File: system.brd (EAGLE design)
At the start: 160 x 100 mm, 122 parts, among them IC1 TPS7B8650BQDDARQ1, IC2 TLV9101IDBVR, IC3 TLV9101IDBVR, J1 TSW-104-07-F-S, J2 163-179PH-EX, J3 RS1-02-G, SW1 1825910-6, SW2 1825910-6, SW3 1825910-6, U1 ATMEGA328PB-AU

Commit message: fixed warnings
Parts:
- SV1: value (none) -> programming pins
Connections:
- removed net N$12: U1.12
- removed net N$13: U1.13
- removed net PC_MCU_RST: TP17.TP
- net PB_MCU_RST: now also TP17.TP
- net PB_MISC1: now also U1.13
- net PB_START: now also U1.12
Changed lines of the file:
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@@
 <drawing>
 <settings>
-<setting alwaysvectorfont="yes"/>
+<setting alwaysvectorfont="no"/>
 <setting verticaltext="up"/>
 </settings>
@@
 <attribute name="VALUE" x="-22.86" y="193.04" size="1.27" layer="27"/>
 </element>
-<element name="SV1" library="con-lstb" library_urn="urn:adsk.eagle:library:162" package="MA04-1" package3d_urn="urn:adsk.eagle:package:8337/1" value="" x="-57.15" y="177.8" smashed="yes">
+<element name="SV1" library="con-lstb" library_urn="urn:adsk.eagle:library:162" package="MA04-1" package3d_urn="urn:adsk.eagle:package:8337/1" value="programming pins" x="-57.15" y="177.8" smashed="yes">
 <attribute name="MF" value="" x="-57.15" y="177.8" size="1.778" layer="27" display="off"/>
 <attribute name="MPN" value="" x="-57.15" y="177.8" size="1.778" layer="27" display="off"/>
@@
 <contactref element="SW3" pad="3"/>
 <contactref element="U1" pad="29"/>
+<contactref element="TP17" pad="TP"/>
+<wire x1="-67.31" y1="191.77" x2="-31.19" y2="159.04" width="0" layer="19" extent="1-1"/>
 <wire x1="-65.17" y1="77.91" x2="-31.19" y2="159.04" width="0" layer="19" extent="1-1"/>
 </signal>
@@
 <contactref element="SW1" pad="3"/>
 <contactref element="TP16" pad="TP"/>
+<contactref element="U1" pad="12"/>
 <wire x1="-123.9" y1="146.34" x2="-60.96" y2="191.77" width="0" layer="19" extent="1-1"/>
-</signal>
-<signal name="N$12">
-<contactref element="U1" pad="12"/>
-</signal>
-<signal name="PB_MISC1">
-<contactref element="SW2" pad="3"/>
-</signal>
-<signal name="N$13">
-<contactref element="U1" pad="13"/>
+<wire x1="-65.17" y1="69.41" x2="-123.9" y2="146.34" width="0" layer="19" extent="1-1"/>
 </signal>
 <signal name="CS_MCU">
@@
 <wire x1="-53.34" y1="177.8" x2="-35.56" y2="191.77" width="0" layer="19" extent="1-1"/>
 <wire x1="-60.52" y1="70.86" x2="-53.34" y2="177.8" width="0" layer="19" extent="1-1"/>
-</signal>
-<signal name="PC_MCU_RST">
-<contactref element="TP17" pad="TP"/>
 </signal>
 <signal name="BATTERY_AND_BUCK:N$2">
@@
 <wire x1="-111.74" y1="169.86" x2="-44.47" y2="174.94" width="0" layer="19" extent="1-1"/>
 </signal>
+<signal name="PB_MISC1">
+<contactref element="SW2" pad="3"/>
+<contactref element="U1" pad="13"/>
+<wire x1="-64.37" y1="69.41" x2="-17.22" y2="157.77" width="0" layer="19" extent="1-1"/>
+</signal>
 </signals>

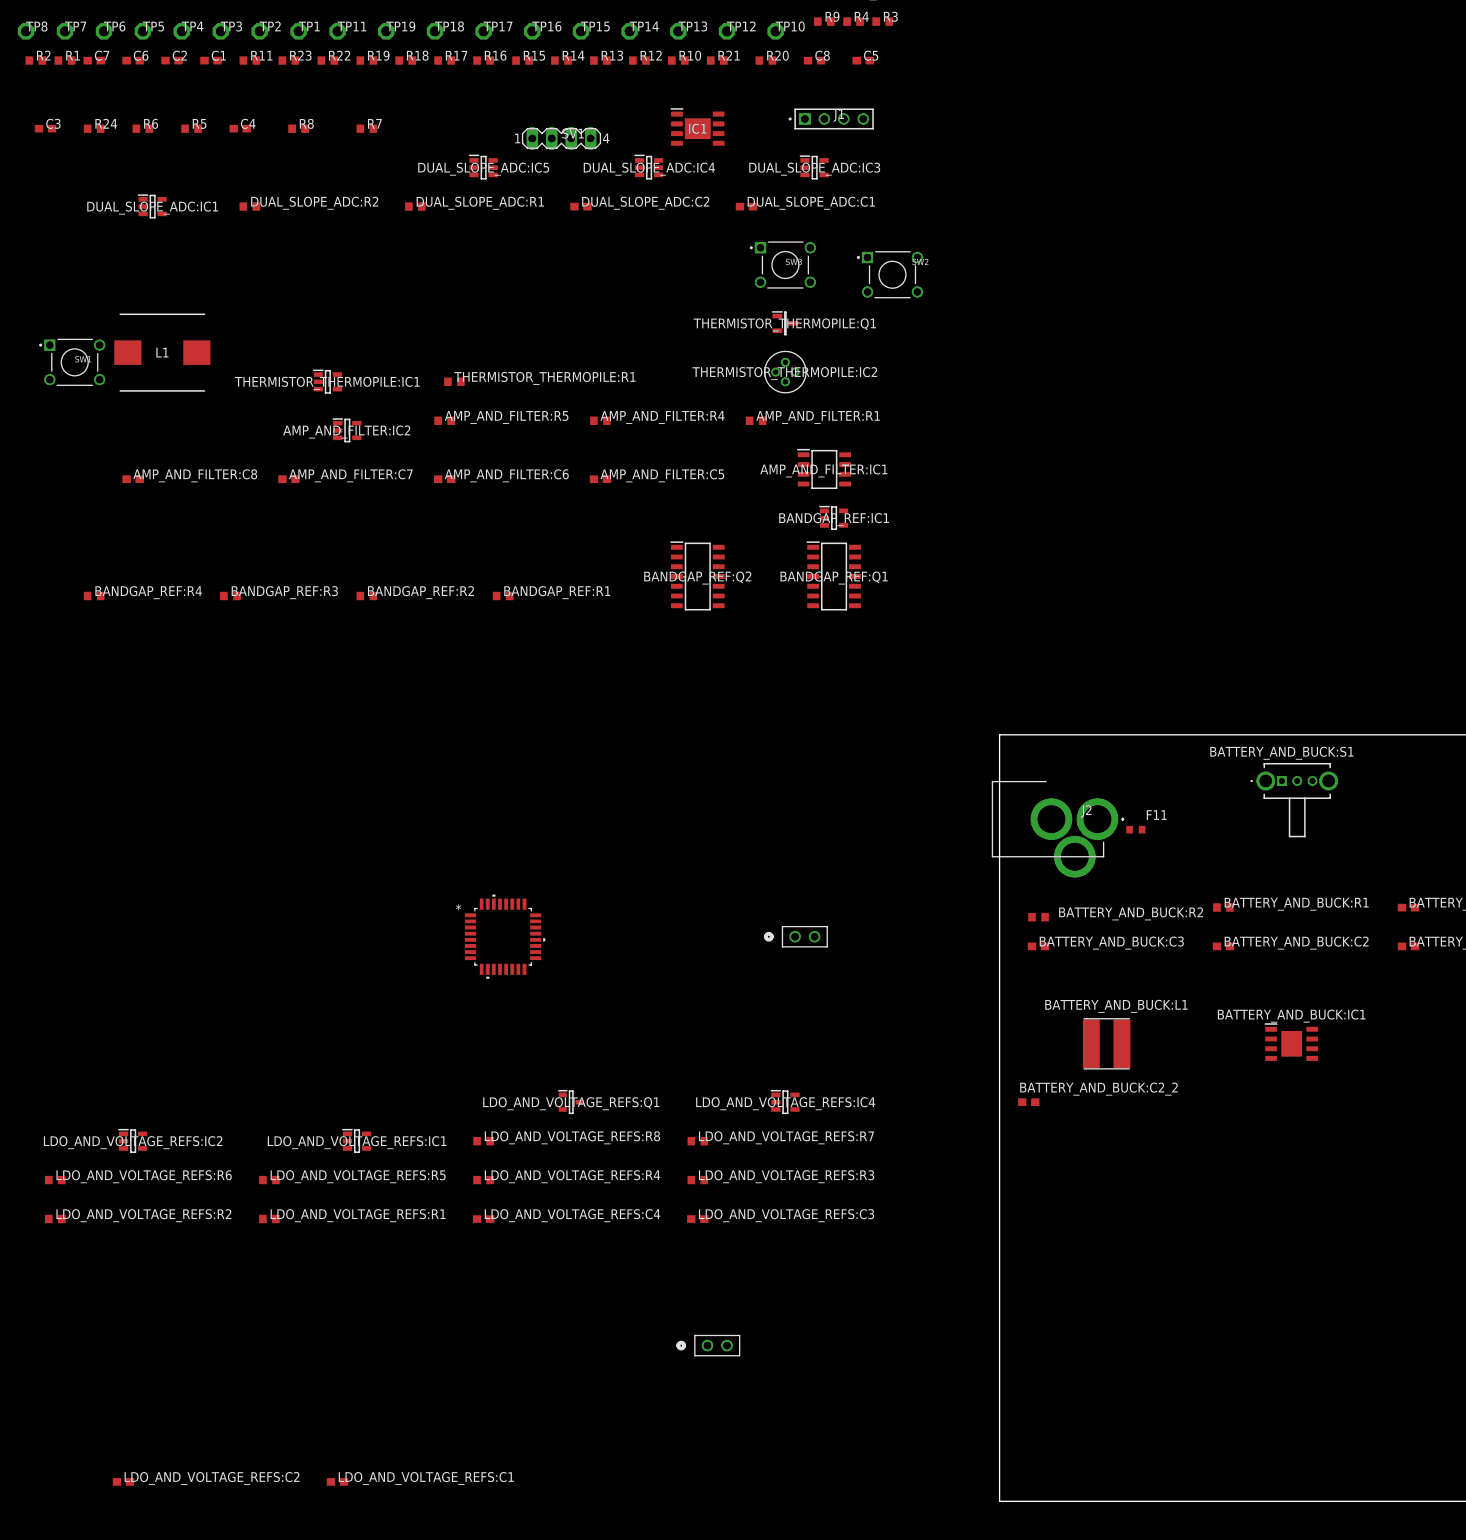
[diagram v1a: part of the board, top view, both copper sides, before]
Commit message: added cap to 2.5V reference
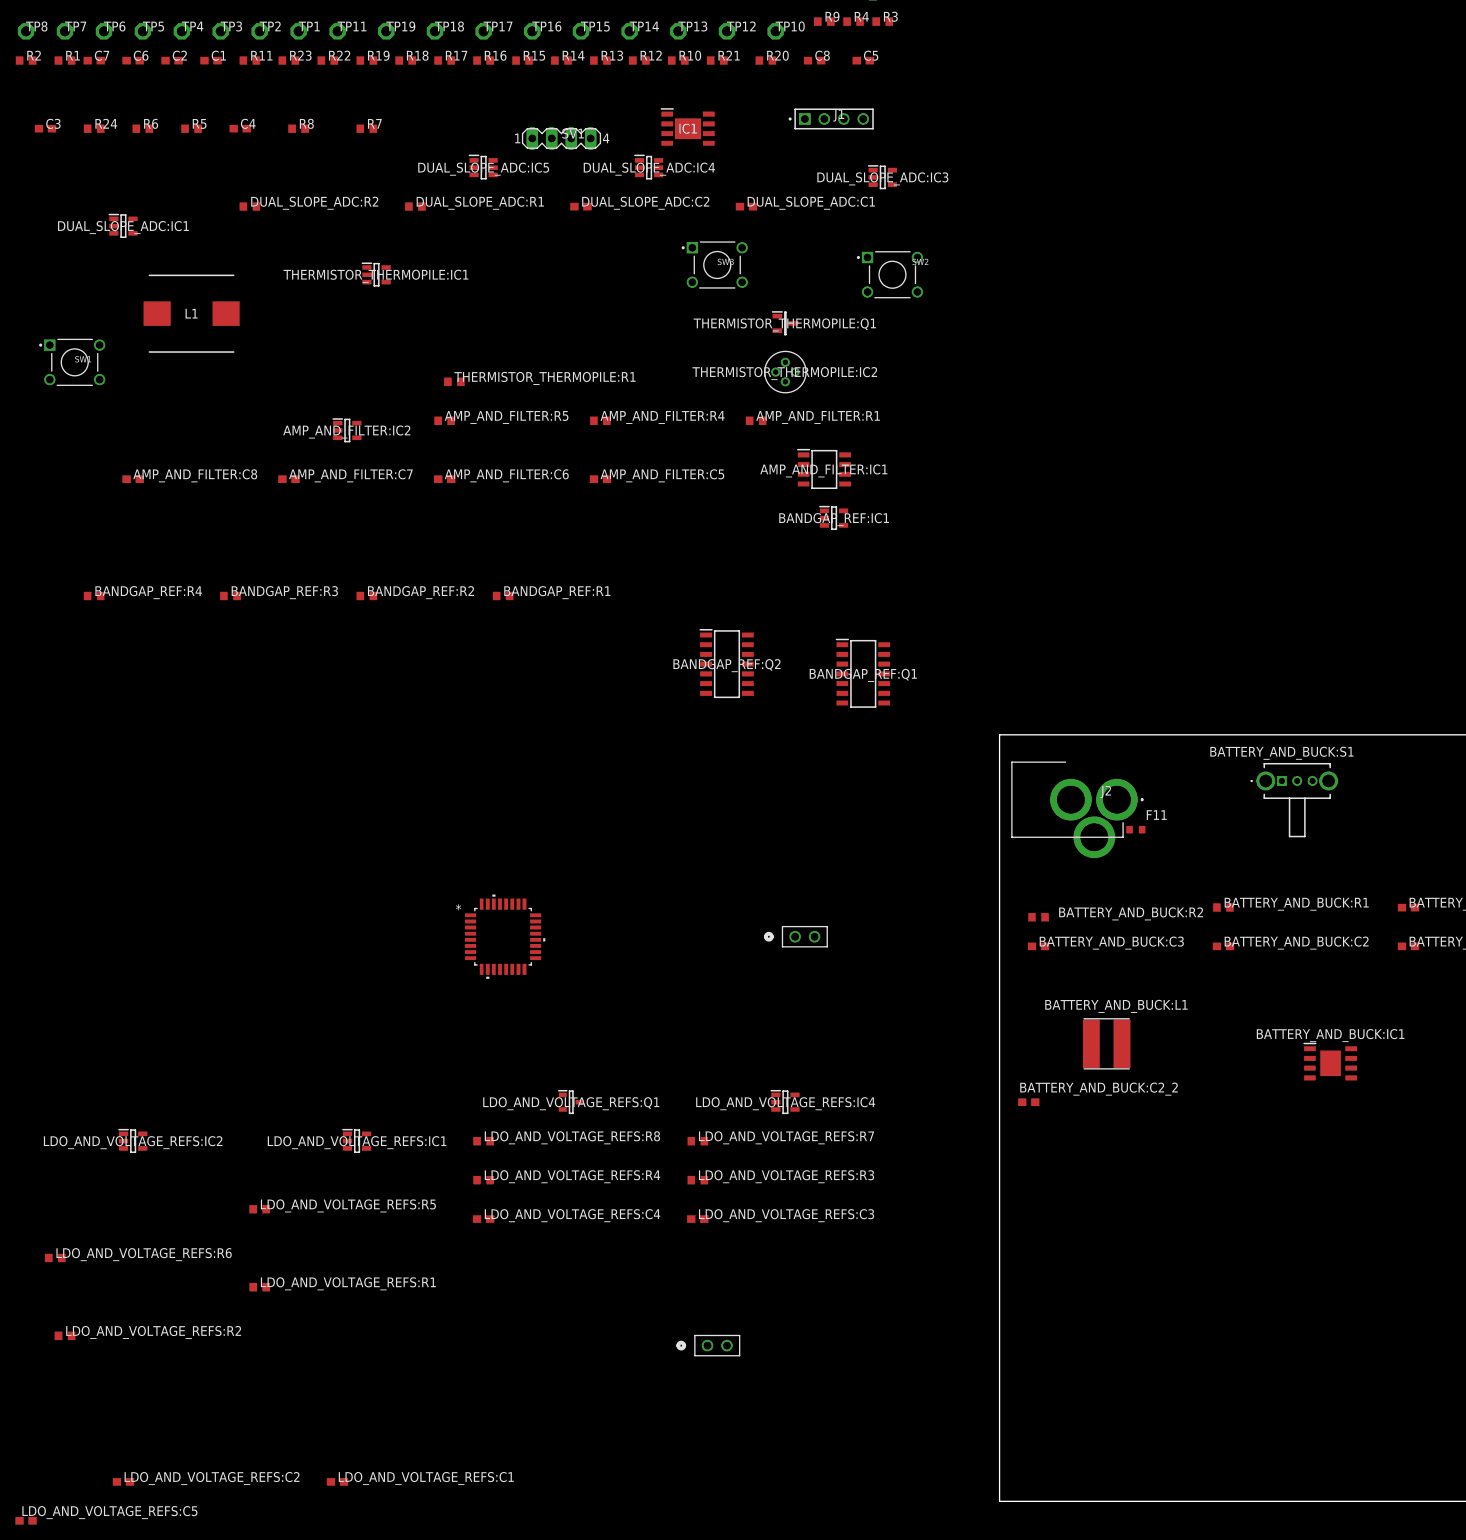
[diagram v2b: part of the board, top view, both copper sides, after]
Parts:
- added LDO_AND_VOLTAGE_REFS:C5: 1uF, rcl:C0603
- moved THERMISTOR_THERMOPILE:IC1 15.3 mm to (-81.3, 160.0)
- moved LDO_AND_VOLTAGE_REFS:R2 15.3 mm to (-121.9, 21.6)
- moved BANDGAP_REF:Q1 13.3 mm to (-17.8, 108.0)
- moved BANDGAP_REF:Q2 12.0 mm to (-35.6, 109.2)
- moved LDO_AND_VOLTAGE_REFS:R6 10.2 mm to (-123.2, 31.8)
- moved DUAL_SLOPE_ADC:IC3 8.98 mm to (-15.2, 172.7)
- moved LDO_AND_VOLTAGE_REFS:R1 8.98 mm to (-96.5, 27.9)
- moved SW3 8.89 mm to (-36.8, 161.3)
- moved L1 6.35 mm to (-105.4, 154.9)
- moved BATTERY_AND_BUCK:IC1 5.68 mm to (43.2, 57.1)
- moved DUAL_SLOPE_ADC:IC1 4.58 mm to (-114.3, 166.4)
- moved LDO_AND_VOLTAGE_REFS:R5 4.02 mm to (-96.5, 38.1)
- moved J2 3.59 mm to (10.2, 90.2)
- moved IC1 1.27 mm to (-40.6, 179.1)
- moved R2 1.27 mm to (-127.0, 188.0)
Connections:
- net 0 renamed GND
- net AMP_AND_FILTER:0 renamed AMP_AND_FILTER:GND
- net BANDGAP_REF:0 renamed BANDGAP_REF:GND
- net BATTERY_AND_BUCK:0 renamed BATTERY_AND_BUCK:GND
- net DUAL_SLOPE_ADC:0 renamed DUAL_SLOPE_ADC:GND
- net THERMISTOR_THERMOPILE:0 renamed THERMISTOR_THERMOPILE:GND
- new net LDO_AND_VOLTAGE_REFS:GND: LDO_AND_VOLTAGE_REFS:C1.2, LDO_AND_VOLTAGE_REFS:C2.2, LDO_AND_VOLTAGE_REFS:C3.2, LDO_AND_VOLTAGE_REFS:C4.2, LDO_AND_VOLTAGE_REFS:IC1.2, LDO_AND_VOLTAGE_REFS:IC2.2, LDO_AND_VOLTAGE_REFS:IC4.2, LDO_AND_VOLTAGE_REFS:J1.2, LDO_AND_VOLTAGE_REFS:R2.1, LDO_AND_VOLTAGE_REFS:R4.1, LDO_AND_VOLTAGE_REFS:R6.1
- net LDO_AND_VOLTAGE_REFS:0: now also LDO_AND_VOLTAGE_REFS:C5.2; no longer LDO_AND_VOLTAGE_REFS:C1.2, LDO_AND_VOLTAGE_REFS:C2.2, LDO_AND_VOLTAGE_REFS:C3.2, LDO_AND_VOLTAGE_REFS:C4.2, LDO_AND_VOLTAGE_REFS:IC1.2, LDO_AND_VOLTAGE_REFS:IC2.2, LDO_AND_VOLTAGE_REFS:IC4.2, LDO_AND_VOLTAGE_REFS:J1.2, LDO_AND_VOLTAGE_REFS:R2.1, LDO_AND_VOLTAGE_REFS:R4.1, LDO_AND_VOLTAGE_REFS:R6.1
- net VS_2.5V: now also LDO_AND_VOLTAGE_REFS:C5.1

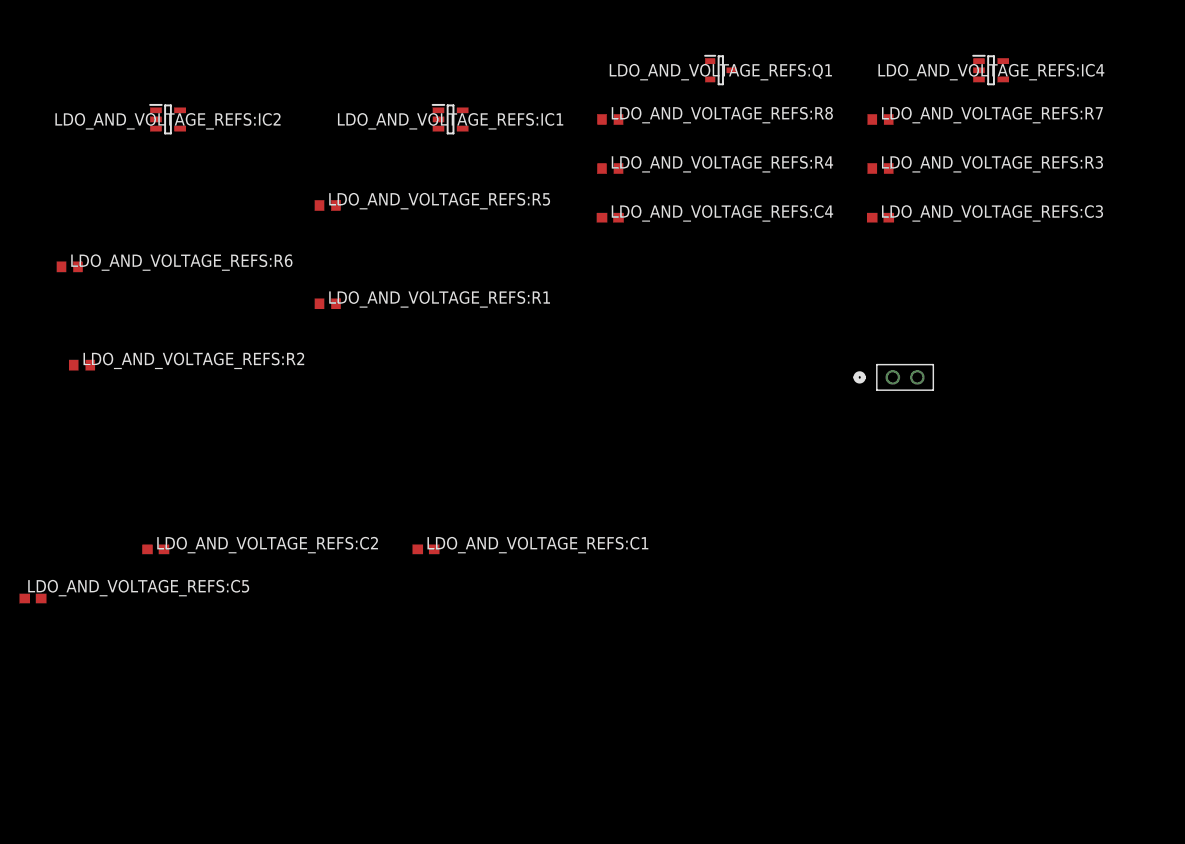
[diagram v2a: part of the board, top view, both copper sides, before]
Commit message: connected grounds. added bypass caps to therm/thermopile + amp&filter
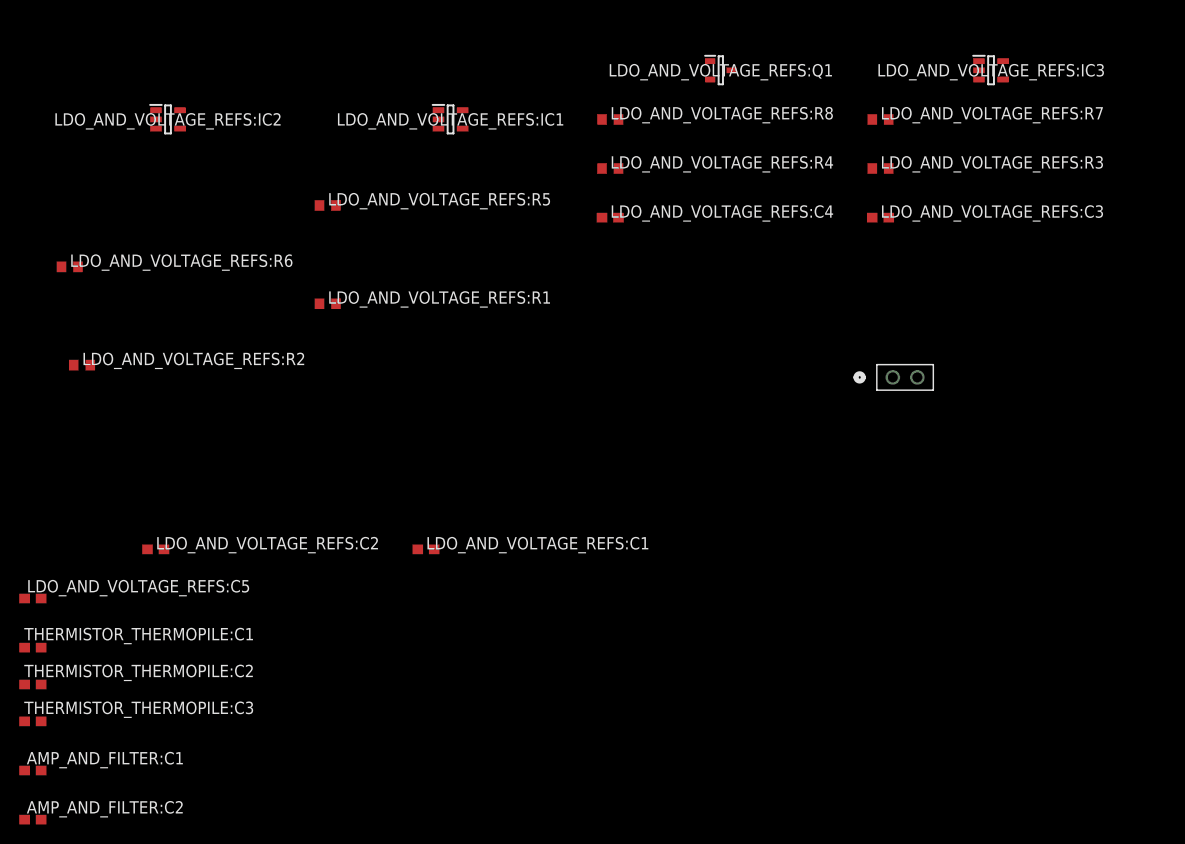
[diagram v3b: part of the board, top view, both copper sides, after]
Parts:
- added AMP_AND_FILTER:C1, AMP_AND_FILTER:C2: 1uF, rcl:C0603
- added THERMISTOR_THERMOPILE:C1, THERMISTOR_THERMOPILE:C2, THERMISTOR_THERMOPILE:C3: 1uF, BeagleBone_Black_Wireless:C0603
- LDO_AND_VOLTAGE_REFS:R5: value 1500 -> 560000
- LDO_AND_VOLTAGE_REFS:R6: value 5000 -> 240000
- R20: value 5000 -> 1500
- R21: value 1500 -> 5000
- renumbered LDO_AND_VOLTAGE_REFS:IC4 to LDO_AND_VOLTAGE_REFS:IC3
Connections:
- new net AMP_AND_FILTER:0: AMP_AND_FILTER:C1.2, AMP_AND_FILTER:C2.2
- new net THERMISTOR_THERMOPILE:0: THERMISTOR_THERMOPILE:C1.2, THERMISTOR_THERMOPILE:C2.2, THERMISTOR_THERMOPILE:C3.2
- net LDO_AND_VOLTAGE_REFS:0: now also LDO_AND_VOLTAGE_REFS:IC3.2
- net LDO_AND_VOLTAGE_REFS:GND: no longer LDO_AND_VOLTAGE_REFS:IC3.2
- net LDO_AND_VOLTAGE_REFS:N$6: now also LDO_AND_VOLTAGE_REFS:IC3.3, LDO_AND_VOLTAGE_REFS:R5.2; no longer LDO_AND_VOLTAGE_REFS:IC3.4, LDO_AND_VOLTAGE_REFS:R5.1
- net VS_1.5V: now also LDO_AND_VOLTAGE_REFS:IC3.4; no longer LDO_AND_VOLTAGE_REFS:R5.2
- net VS_2.5V_OUT: now also AMP_AND_FILTER:C2.1, THERMISTOR_THERMOPILE:C3.1
- net VS_5V: now also LDO_AND_VOLTAGE_REFS:R5.1
- net VS_5V_OUT: now also AMP_AND_FILTER:C1.1, THERMISTOR_THERMOPILE:C1.1, THERMISTOR_THERMOPILE:C2.1
- net V_BG: no longer LDO_AND_VOLTAGE_REFS:IC3.3

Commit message: Fixed grounds issue
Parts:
- removed TP12, TP15, TP18: TPPAD1-13, testpad:P1-13
- R24: value 20000 -> 100000
- moved BATTERY_AND_BUCK:RT 198.1 mm to (-132.1, 90.2)
- moved BATTERY_AND_BUCK:C6 187.2 mm to (-132.1, 102.9)
- moved BATTERY_AND_BUCK:C5 178.4 mm to (-108.0, 102.9)
- moved THERMISTOR_THERMOPILE:C1 177.9 mm to (-71.1, 161.3)
- moved THERMISTOR_THERMOPILE:C3 176.5 mm to (-129.5, 161.3)
- moved THERMISTOR_THERMOPILE:C2 174.8 mm to (-100.3, 161.3)
- moved BATTERY_AND_BUCK:R5 155.5 mm to (-83.8, 108.0)
- moved AMP_AND_FILTER:C1 153.0 mm to (-52.1, 113.0)
- moved AMP_AND_FILTER:C2 148.8 mm to (-72.4, 113.0)
- moved F11 148.3 mm to (-82.5, 196.8)
- moved BATTERY_AND_BUCK:IC1 120.5 mm to (-72.4, 91.4)
- moved BATTERY_AND_BUCK:C2_2 118.1 mm to (-108.0, 90.2)
- moved C3 110.0 mm to (-17.8, 205.7)
- moved IC2 97.4 mm to (-121.9, 210.8)
- moved TP9 97.4 mm to (-113.0, 209.6)
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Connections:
- removed net AMP_AND_FILTER:0: AMP_AND_FILTER:C1.2, AMP_AND_FILTER:C2.2
- removed net AMP_AND_FILTER:GND: AMP_AND_FILTER:C5.2, AMP_AND_FILTER:C8.2, AMP_AND_FILTER:IC1.4, AMP_AND_FILTER:IC2.2
- removed net BANDGAP_REF:GND: BANDGAP_REF:IC1.2, BANDGAP_REF:Q1.5, BANDGAP_REF:Q2.10, BANDGAP_REF:Q2.12, BANDGAP_REF:Q2.3, BANDGAP_REF:Q2.5
- removed net BATTERY_AND_BUCK:GND: BATTERY_AND_BUCK:C1.2, BATTERY_AND_BUCK:C2_2.2, BATTERY_AND_BUCK:C5.2, BATTERY_AND_BUCK:C6.2, BATTERY_AND_BUCK:IC1.7, BATTERY_AND_BUCK:IC1.9, BATTERY_AND_BUCK:R2.1, BATTERY_AND_BUCK:RT.1, BATTERY_AND_BUCK:S1.3
- removed net CS_MCU: SV1.1, TP15.TP, U1.14
- removed net DUAL_SLOPE_ADC:GND: DUAL_SLOPE_ADC:C2.2, DUAL_SLOPE_ADC:IC1.2, DUAL_SLOPE_ADC:IC3.2, DUAL_SLOPE_ADC:IC4.3, DUAL_SLOPE_ADC:IC5.3
- removed net GND: C1.2, C2.2, C3.2, C4.2, C5.2, C6.2, C7.2, C8.2, IC1.5, IC1.9, IC2.2, IC3.2, J1.01, J2.B, J2.C, J3.1, R21.1, R4.1, R8.1, SW1.1, SW2.1, SW3.1, U1.21, U1.5
- removed net LDO_AND_VOLTAGE_REFS:0: LDO_AND_VOLTAGE_REFS:C5.2, LDO_AND_VOLTAGE_REFS:IC3.2
- removed net LDO_AND_VOLTAGE_REFS:GND: LDO_AND_VOLTAGE_REFS:C1.2, LDO_AND_VOLTAGE_REFS:C2.2, LDO_AND_VOLTAGE_REFS:C3.2, LDO_AND_VOLTAGE_REFS:C4.2, LDO_AND_VOLTAGE_REFS:IC1.2, LDO_AND_VOLTAGE_REFS:IC2.2, LDO_AND_VOLTAGE_REFS:J1.2, LDO_AND_VOLTAGE_REFS:R2.1, LDO_AND_VOLTAGE_REFS:R4.1, LDO_AND_VOLTAGE_REFS:R6.1
- removed net PB_MCU_RST: SW3.3, TP17.TP, U1.29
- removed net THERMISTOR_THERMOPILE:0: THERMISTOR_THERMOPILE:C1.2, THERMISTOR_THERMOPILE:C2.2, THERMISTOR_THERMOPILE:C3.2
- removed net THERMISTOR_THERMOPILE:GND: THERMISTOR_THERMOPILE:IC1.2, THERMISTOR_THERMOPILE:IC2.1
- new net 0: AMP_AND_FILTER:C1.2, AMP_AND_FILTER:C2.2, AMP_AND_FILTER:C5.2, AMP_AND_FILTER:C8.2, AMP_AND_FILTER:IC1.4, AMP_AND_FILTER:IC2.2, BANDGAP_REF:IC1.2, BANDGAP_REF:Q1.5, BANDGAP_REF:Q2.10, BANDGAP_REF:Q2.12, BANDGAP_REF:Q2.3, BANDGAP_REF:Q2.5, BATTERY_AND_BUCK:C1.2, BATTERY_AND_BUCK:C2_2.2, BATTERY_AND_BUCK:C5.2, BATTERY_AND_BUCK:C6.2, BATTERY_AND_BUCK:IC1.7, BATTERY_AND_BUCK:IC1.9, BATTERY_AND_BUCK:R2.1, BATTERY_AND_BUCK:RT.1, BATTERY_AND_BUCK:S1.3, C1.2, C2.2, C3.2, C4.2, C5.2, C6.2, C7.2, C8.2, DUAL_SLOPE_ADC:C2.2, DUAL_SLOPE_ADC:IC1.2, DUAL_SLOPE_ADC:IC3.2, DUAL_SLOPE_ADC:IC4.3, DUAL_SLOPE_ADC:IC5.3, IC1.5, IC1.9, IC2.2, IC3.2, J1.01, J2.B, J2.C, J3.1, LDO_AND_VOLTAGE_REFS:C1.2, LDO_AND_VOLTAGE_REFS:C2.2, LDO_AND_VOLTAGE_REFS:C3.2, LDO_AND_VOLTAGE_REFS:C4.2, LDO_AND_VOLTAGE_REFS:C5.2, LDO_AND_VOLTAGE_REFS:IC1.2, LDO_AND_VOLTAGE_REFS:IC2.2, LDO_AND_VOLTAGE_REFS:IC3.2, LDO_AND_VOLTAGE_REFS:J1.2, LDO_AND_VOLTAGE_REFS:R2.1, LDO_AND_VOLTAGE_REFS:R4.1, LDO_AND_VOLTAGE_REFS:R6.1, R21.1, R4.1, R8.1, SW1.1, SW2.1, SW3.1, THERMISTOR_THERMOPILE:C1.2, THERMISTOR_THERMOPILE:C2.2, THERMISTOR_THERMOPILE:C3.2, THERMISTOR_THERMOPILE:IC1.2, THERMISTOR_THERMOPILE:IC2.1, U1.21, U1.5
- new net MCU_RST: SV1.1, SW3.3, TP17.TP, U1.29
- net SCK_MCU: no longer TP12.TP
- net SCL: no longer TP18.TP
